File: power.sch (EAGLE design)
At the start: 26 parts

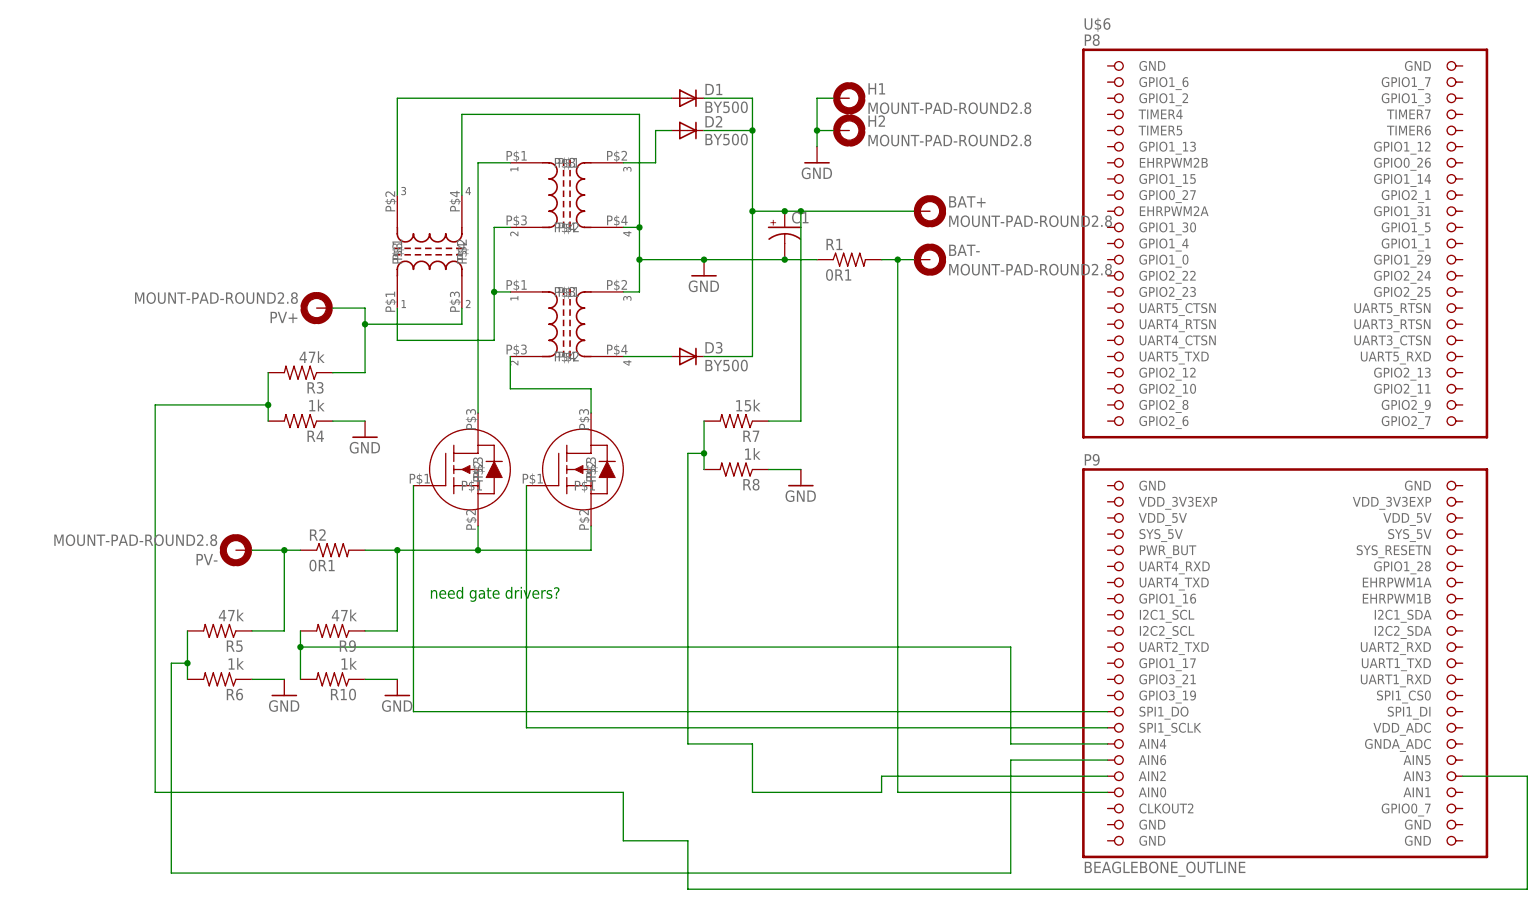
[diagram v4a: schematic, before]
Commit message: better ground paths
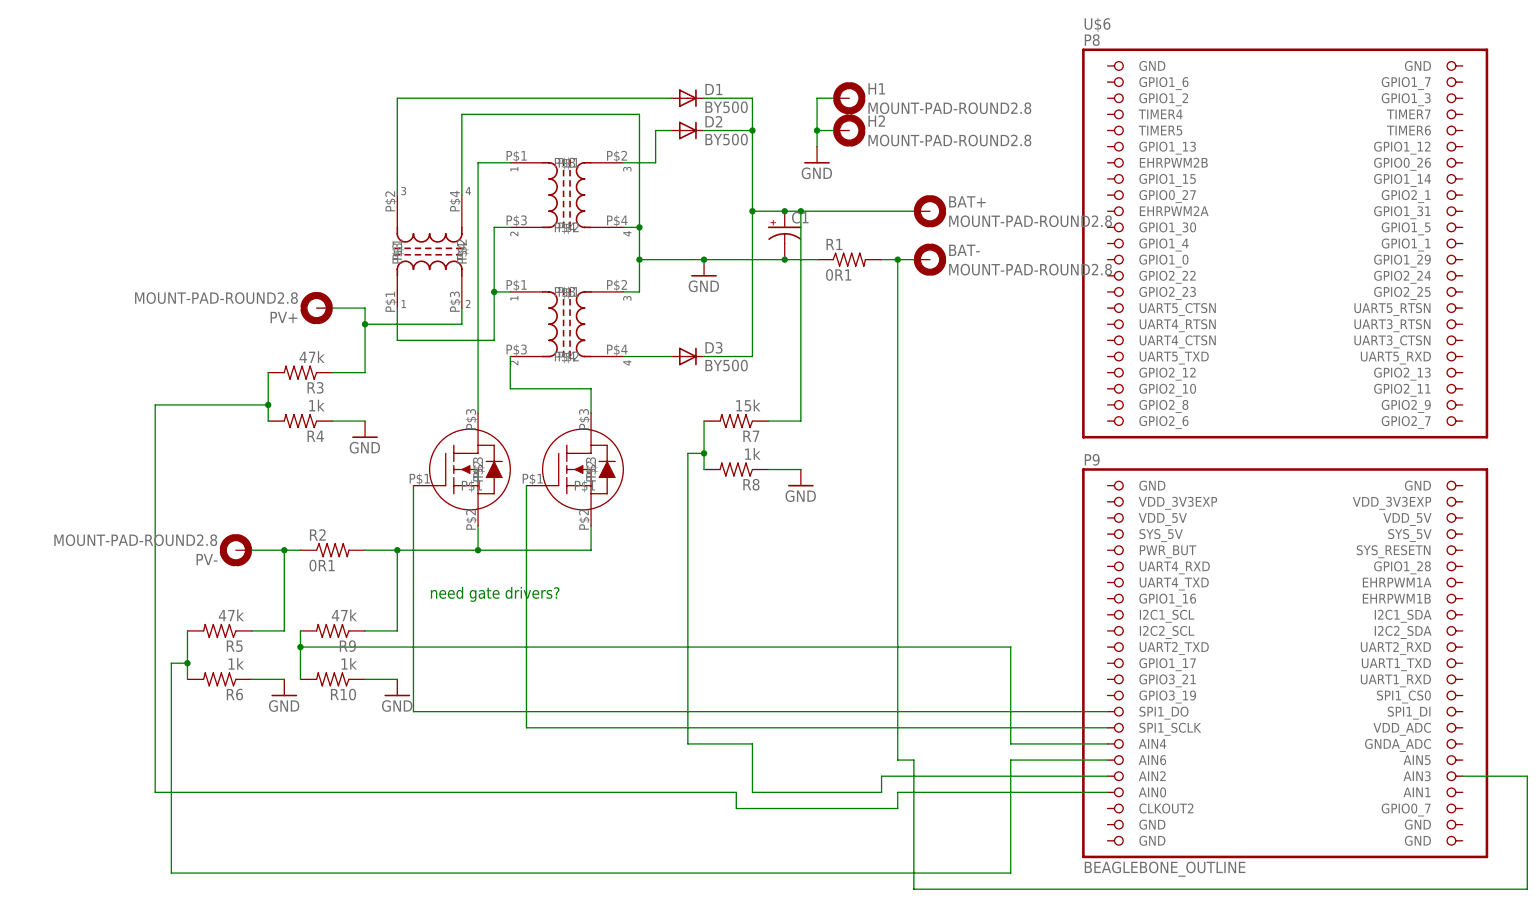
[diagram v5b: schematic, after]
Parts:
- C1: device rcl:CPOL-USE3.5-8 -> rcl:CPOL-USE5-10.5
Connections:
- net N$12: now also R3.2, R4.2; no longer BAT-.MOUNT, R1.2
- net N$4: now also BAT-.MOUNT, R1.2; no longer R3.2, R4.2
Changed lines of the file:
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@@
 <grid distance="0.1" unitdist="inch" unit="inch" style="lines" multiple="1" display="no" altdistance="0.01" altunitdist="inch" altunit="inch"/>
 <layers>
-<layer number="1" name="Top" color="4" fill="1" visible="no" active="no"/>
-<layer number="16" name="Bottom" color="1" fill="1" visible="no" active="no"/>
-<layer number="17" name="Pads" color="2" fill="1" visible="no" active="no"/>
-<layer number="18" name="Vias" color="2" fill="1" visible="no" active="no"/>
-<layer number="19" name="Unrouted" color="6" fill="1" visible="no" active="no"/>
-<layer number="20" name="Dimension" color="15" fill="1" visible="no" active="no"/>
-<layer number="21" name="tPlace" color="7" fill="1" visible="no" active="no"/>
-<layer number="22" name="bPlace" color="7" fill="1" visible="no" active="no"/>
-<layer number="23" name="tOrigins" color="15" fill="1" visible="no" active="no"/>
-<layer number="24" name="bOrigins" color="15" fill="1" visible="no" active="no"/>
-<layer number="25" name="tNames" color="7" fill="1" visible="no" active="no"/>
-<layer number="26" name="bNames" color="7" fill="1" visible="no" active="no"/>
-<layer number="27" name="tValues" color="7" fill="1" visible="no" active="no"/>
-<layer number="28" name="bValues" color="7" fill="1" visible="no" active="no"/>
+<layer number="1" name="Top" color="4" fill="1" visible="yes" active="no"/>
+<layer number="16" name="Bottom" color="1" fill="1" visible="yes" active="no"/>
+<layer number="17" name="Pads" color="2" fill="1" visible="yes" active="no"/>
+<layer number="18" name="Vias" color="2" fill="1" visible="yes" active="no"/>
+<layer number="19" name="Unrouted" color="6" fill="1" visible="yes" active="no"/>
+<layer number="20" name="Dimension" color="15" fill="1" visible="yes" active="no"/>
+<layer number="21" name="tPlace" color="7" fill="1" visible="yes" active="no"/>
+<layer number="22" name="bPlace" color="7" fill="1" visible="yes" active="no"/>
+<layer number="23" name="tOrigins" color="15" fill="1" visible="yes" active="no"/>
+<layer number="24" name="bOrigins" color="15" fill="1" visible="yes" active="no"/>
+<layer number="25" name="tNames" color="7" fill="1" visible="yes" active="no"/>
+<layer number="26" name="bNames" color="7" fill="1" visible="yes" active="no"/>
+<layer number="27" name="tValues" color="7" fill="1" visible="yes" active="no"/>
+<layer number="28" name="bValues" color="7" fill="1" visible="yes" active="no"/>
 <layer number="29" name="tStop" color="7" fill="3" visible="no" active="no"/>
 <layer number="30" name="bStop" color="7" fill="6" visible="no" active="no"/>
@@
 <layer number="35" name="tGlue" color="7" fill="4" visible="no" active="no"/>
 <layer number="36" name="bGlue" color="7" fill="5" visible="no" active="no"/>
-<layer number="37" name="tTest" color="7" fill="1" visible="no" active="no"/>
-<layer number="38" name="bTest" color="7" fill="1" visible="no" active="no"/>
+<layer number="37" name="tTest" color="7" fill="1" visible="yes" active="no"/>
+<layer number="38" name="bTest" color="7" fill="1" visible="yes" active="no"/>
 <layer number="39" name="tKeepout" color="4" fill="11" visible="no" active="no"/>
 <layer number="40" name="bKeepout" color="1" fill="11" visible="no" active="no"/>
@@
 <layer number="44" name="Drills" color="7" fill="1" visible="no" active="no"/>
 <layer number="45" name="Holes" color="7" fill="1" visible="no" active="no"/>
-<layer number="46" name="Milling" color="3" fill="1" visible="no" active="no"/>
-<layer number="47" name="Measures" color="7" fill="1" visible="no" active="no"/>
-<layer number="48" name="Document" color="7" fill="1" visible="no" active="no"/>
-<layer number="49" name="Reference" color="7" fill="1" visible="no" active="no"/>
-<layer number="50" name="dxf" color="7" fill="1" visible="no" active="no"/>
-<layer number="51" name="tDocu" color="7" fill="1" visible="no" active="no"/>
-<layer number="52" name="bDocu" color="7" fill="1" visible="no" active="no"/>
-<layer number="53" name="tGND_GNDA" color="7" fill="9" visible="no" active="no"/>
-<layer number="54" name="bGND_GNDA" color="1" fill="9" visible="no" active="no"/>
-<layer number="56" name="wert" color="7" fill="1" visible="no" active="no"/>
-<layer number="57" name="tCAD" color="7" fill="1" visible="no" active="no"/>
+<layer number="46" name="Milling" color="3" fill="1" visible="yes" active="no"/>
+<layer number="47" name="Measures" color="7" fill="1" visible="yes" active="no"/>
+<layer number="48" name="Document" color="7" fill="1" visible="yes" active="no"/>
+<layer number="49" name="Reference" color="7" fill="1" visible="yes" active="no"/>
+<layer number="50" name="dxf" color="7" fill="1" visible="yes" active="no"/>
+<layer number="51" name="tDocu" color="7" fill="1" visible="yes" active="no"/>
+<layer number="52" name="bDocu" color="7" fill="1" visible="yes" active="no"/>
+<layer number="53" name="tGND_GNDA" color="7" fill="9" visible="yes" active="no"/>
+<layer number="54" name="bGND_GNDA" color="1" fill="9" visible="yes" active="no"/>
+<layer number="56" name="wert" color="7" fill="1" visible="yes" active="no"/>
+<layer number="57" name="tCAD" color="7" fill="1" visible="yes" active="no"/>
 <layer number="91" name="Nets" color="2" fill="1" visible="yes" active="yes"/>
 <layer number="92" name="Busses" color="1" fill="1" visible="yes" active="yes"/>
@@
 <part name="D2" library="diode" deviceset="BY500" device=""/>
 <part name="D3" library="diode" deviceset="BY500" device=""/>
-<part name="C1" library="rcl" deviceset="CPOL-US" device="E3.5-8"/>
+<part name="C1" library="rcl" deviceset="CPOL-US" device="E5-10.5"/>
 <part name="U$1" library="mjg" deviceset="FDB6670AL" device=""/>
 <part name="U$2" library="mjg" deviceset="FDB6670AL" device=""/>
@@
 <net name="N$4" class="0">
 <segment>
-<pinref part="R3" gate="G$1" pin="2"/>
-<pinref part="R4" gate="G$1" pin="2"/>
-<wire x1="-7.62" y1="33.02" x2="-7.62" y2="27.94" width="0.1524" layer="91"/>
-<wire x1="-7.62" y1="27.94" x2="-7.62" y2="25.4" width="0.1524" layer="91"/>
-<wire x1="-7.62" y1="27.94" x2="-25.4" y2="27.94" width="0.1524" layer="91"/>
-<wire x1="-25.4" y1="27.94" x2="-25.4" y2="-33.02" width="0.1524" layer="91"/>
-<junction x="-7.62" y="27.94"/>
-<wire x1="-25.4" y1="-33.02" x2="48.26" y2="-33.02" width="0.1524" layer="91"/>
-<wire x1="58.42" y1="-40.64" x2="58.42" y2="-48.26" width="0.1524" layer="91"/>
-<wire x1="58.42" y1="-48.26" x2="190.5" y2="-48.26" width="0.1524" layer="91"/>
 <pinref part="U$6" gate="G$1" pin="AIN3"/>
+<wire x1="93.98" y1="-48.26" x2="190.5" y2="-48.26" width="0.1524" layer="91"/>
 <wire x1="190.5" y1="-48.26" x2="190.5" y2="-30.48" width="0.1524" layer="91"/>
 <wire x1="190.5" y1="-30.48" x2="180.34" y2="-30.48" width="0.1524" layer="91"/>
-<wire x1="48.26" y1="-33.02" x2="48.26" y2="-40.64" width="0.1524" layer="91"/>
-<wire x1="48.26" y1="-40.64" x2="58.42" y2="-40.64" width="0.1524" layer="91"/>
+<pinref part="BAT-" gate="G$1" pin="MOUNT"/>
+<pinref part="R1" gate="G$1" pin="2"/>
+<wire x1="88.9" y1="50.8" x2="91.44" y2="50.8" width="0.1524" layer="91"/>
+<wire x1="91.44" y1="50.8" x2="93.98" y2="50.8" width="0.1524" layer="91"/>
+<junction x="91.44" y="50.8"/>
+<wire x1="91.44" y1="50.8" x2="91.44" y2="-27.94" width="0.1524" layer="91"/>
+<wire x1="91.44" y1="-27.94" x2="93.98" y2="-27.94" width="0.1524" layer="91"/>
+<wire x1="93.98" y1="-27.94" x2="93.98" y2="-48.26" width="0.1524" layer="91"/>
 </segment>
 </net>
@@
 </segment>
 </net>
-<net name="N$12" class="0">
-<segment>
-<pinref part="U$6" gate="G$1" pin="AIN0"/>
-<wire x1="91.44" y1="-33.02" x2="124.46" y2="-33.02" width="0.1524" layer="91"/>
-<pinref part="BAT-" gate="G$1" pin="MOUNT"/>
-<pinref part="R1" gate="G$1" pin="2"/>
-<wire x1="88.9" y1="50.8" x2="91.44" y2="50.8" width="0.1524" layer="91"/>
-<wire x1="91.44" y1="50.8" x2="93.98" y2="50.8" width="0.1524" layer="91"/>
-<junction x="91.44" y="50.8"/>
-<wire x1="91.44" y1="50.8" x2="91.44" y2="-33.02" width="0.1524" layer="91"/>
-</segment>
-</net>
 <net name="N$10" class="0">
 <segment>
@@
 </segment>
 </net>
+<net name="N$12" class="0">
+<segment>
+<pinref part="U$6" gate="G$1" pin="AIN0"/>
+<wire x1="91.44" y1="-33.02" x2="124.46" y2="-33.02" width="0.1524" layer="91"/>
+<wire x1="91.44" y1="-35.56" x2="91.44" y2="-33.02" width="0.1524" layer="91"/>
+<wire x1="66.04" y1="-35.56" x2="91.44" y2="-35.56" width="0.1524" layer="91"/>
+<wire x1="66.04" y1="-33.02" x2="66.04" y2="-35.56" width="0.1524" layer="91"/>
+<wire x1="-25.4" y1="-33.02" x2="66.04" y2="-33.02" width="0.1524" layer="91"/>
+<pinref part="R4" gate="G$1" pin="2"/>
+<pinref part="R3" gate="G$1" pin="2"/>
+<wire x1="-7.62" y1="33.02" x2="-7.62" y2="27.94" width="0.1524" layer="91"/>
+<wire x1="-7.62" y1="27.94" x2="-7.62" y2="25.4" width="0.1524" layer="91"/>
+<junction x="-7.62" y="27.94"/>
+<wire x1="-7.62" y1="27.94" x2="-25.4" y2="27.94" width="0.1524" layer="91"/>
+<wire x1="-25.4" y1="27.94" x2="-25.4" y2="-33.02" width="0.1524" layer="91"/>
+</segment>
+</net>

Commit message: fixed a lot of things.  confidence that this could work is up to 1%.
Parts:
- removed H2: MOUNT-PAD-ROUND2.8, holes:MOUNT-PAD-ROUND2.8
- removed R7: 15k, rcl:R-US_R0603
- removed U$1, U$2: FDB6670AL, mjg:FDB6670AL
- added U$7, U$8: 45NO6LG, semiconductors:45NO6LG
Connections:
- net GND: no longer H2.MOUNT
- net N$10: no longer R7.2
- net N$11: now also U$6.SPI1_DO, U$8.G; no longer U$2.P$1, U$6.SPI1_SCLK
- net N$13: now also U$6.SPI1_SCLK, U$7.G; no longer U$1.P$1, U$6.SPI1_DO
- net N$15: now also U$7.D; no longer U$1.P$2
- net N$5: now also U$8.D; no longer U$2.P$2
- net N$7: no longer R7.1
- net N$8: now also U$8.S; no longer U$1.P$3, U$2.P$3
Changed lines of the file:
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@@
 <part name="D3" library="diode" deviceset="BY500" device=""/>
 <part name="C1" library="rcl" deviceset="CPOL-US" device="E5-10.5"/>
-<part name="U$1" library="mjg" deviceset="FDB6670AL" device=""/>
-<part name="U$2" library="mjg" deviceset="FDB6670AL" device=""/>
 <part name="R1" library="rcl" deviceset="R-US_" device="R0603" value="0R1"/>
 <part name="R2" library="rcl" deviceset="R-US_" device="R0603" value="0R1"/>
@@
 <part name="R6" library="rcl" deviceset="R-US_" device="R0603" value="1k"/>
 <part name="GND3" library="supply1" deviceset="GND" device=""/>
-<part name="R7" library="rcl" deviceset="R-US_" device="R0603" value="15k"/>
 <part name="R8" library="rcl" deviceset="R-US_" device="R0603" value="1k"/>
 <part name="GND4" library="supply1" deviceset="GND" device=""/>
@@
 <part name="BAT-" library="holes" deviceset="MOUNT-PAD-ROUND" device="2.8"/>
 <part name="H1" library="holes" deviceset="MOUNT-PAD-ROUND" device="2.8"/>
-<part name="H2" library="holes" deviceset="MOUNT-PAD-ROUND" device="2.8"/>
 <part name="GND6" library="supply1" deviceset="GND" device=""/>
+<part name="U$7" library="semiconductors" deviceset="45NO6LG" device=""/>
+<part name="U$8" library="semiconductors" deviceset="45NO6LG" device=""/>
 </parts>
 <sheets>
@@
 <instance part="D3" gate="1" x="58.42" y="35.56"/>
 <instance part="C1" gate="G$1" x="73.66" y="55.88"/>
-<instance part="U$1" gate="G$1" x="24.13" y="17.78"/>
-<instance part="U$2" gate="G$1" x="41.91" y="17.78"/>
 <instance part="R1" gate="G$1" x="83.82" y="50.8"/>
 <instance part="R2" gate="G$1" x="2.54" y="5.08"/>
@@
 <instance part="R6" gate="G$1" x="-15.24" y="-15.24" rot="R180"/>
 <instance part="GND3" gate="1" x="-5.08" y="-17.78"/>
-<instance part="R7" gate="G$1" x="66.04" y="25.4" rot="R180"/>
 <instance part="R8" gate="G$1" x="66.04" y="17.78" rot="R180"/>
 <instance part="GND4" gate="1" x="76.2" y="15.24"/>
@@
 <instance part="BAT-" gate="G$1" x="96.52" y="50.8"/>
 <instance part="H1" gate="G$1" x="83.82" y="76.2"/>
-<instance part="H2" gate="G$1" x="83.82" y="71.12"/>
 <instance part="GND6" gate="1" x="78.74" y="66.04"/>
+<instance part="U$7" gate="G$1" x="22.86" y="17.78"/>
+<instance part="U$8" gate="G$1" x="40.64" y="17.78"/>
 </instances>
 <busses>
@@
 <net name="N$5" class="0">
 <segment>
-<pinref part="U$2" gate="G$1" pin="P$2"/>
-<wire x1="43.18" y1="26.67" x2="43.18" y2="30.48" width="0.1524" layer="91"/>
 <pinref part="U$4" gate="G$1" pin="P$2"/>
 <wire x1="30.48" y1="35.56" x2="30.48" y2="30.48" width="0.1524" layer="91"/>
 <wire x1="30.48" y1="30.48" x2="43.18" y2="30.48" width="0.1524" layer="91"/>
+<pinref part="U$8" gate="G$1" pin="D"/>
+<wire x1="43.18" y1="30.48" x2="43.18" y2="22.86" width="0.1524" layer="91"/>
 </segment>
 </net>
 <net name="N$13" class="0">
 <segment>
-<pinref part="U$1" gate="G$1" pin="P$1"/>
-<pinref part="U$6" gate="G$1" pin="SPI1_DO"/>
-<wire x1="15.24" y1="-20.32" x2="15.24" y2="15.24" width="0.1524" layer="91"/>
-<wire x1="124.46" y1="-20.32" x2="15.24" y2="-20.32" width="0.1524" layer="91"/>
+<wire x1="15.24" y1="-22.86" x2="15.24" y2="15.24" width="0.1524" layer="91"/>
+<pinref part="U$7" gate="G$1" pin="G"/>
+<wire x1="15.24" y1="15.24" x2="20.32" y2="15.24" width="0.1524" layer="91"/>
+<pinref part="U$6" gate="G$1" pin="SPI1_SCLK"/>
+<wire x1="124.46" y1="-22.86" x2="15.24" y2="-22.86" width="0.1524" layer="91"/>
 </segment>
 </net>
@@
 <pinref part="U$5" gate="G$1" pin="P$1"/>
 <wire x1="30.48" y1="66.04" x2="25.4" y2="66.04" width="0.1524" layer="91"/>
-<pinref part="U$1" gate="G$1" pin="P$2"/>
-<wire x1="25.4" y1="66.04" x2="25.4" y2="26.67" width="0.1524" layer="91"/>
+<wire x1="25.4" y1="66.04" x2="25.4" y2="22.86" width="0.1524" layer="91"/>
+<pinref part="U$7" gate="G$1" pin="D"/>
 </segment>
 </net>
@@
 <wire x1="81.28" y1="76.2" x2="78.74" y2="76.2" width="0.1524" layer="91"/>
 <wire x1="78.74" y1="76.2" x2="78.74" y2="71.12" width="0.1524" layer="91"/>
-<pinref part="H2" gate="G$1" pin="MOUNT"/>
 <wire x1="78.74" y1="71.12" x2="78.74" y2="68.58" width="0.1524" layer="91"/>
 <wire x1="81.28" y1="71.12" x2="78.74" y2="71.12" width="0.1524" layer="91"/>
@@
 <net name="N$7" class="0">
 <segment>
-<pinref part="R7" gate="G$1" pin="1"/>
 <wire x1="76.2" y1="25.4" x2="71.12" y2="25.4" width="0.1524" layer="91"/>
 <pinref part="D1" gate="1" pin="C"/>
@@
 <pinref part="R9" gate="G$1" pin="1"/>
 <wire x1="12.7" y1="-7.62" x2="7.62" y2="-7.62" width="0.1524" layer="91"/>
-<pinref part="U$1" gate="G$1" pin="P$3"/>
-<wire x1="25.4" y1="8.89" x2="25.4" y2="5.08" width="0.1524" layer="91"/>
-<wire x1="25.4" y1="5.08" x2="43.18" y2="5.08" width="0.1524" layer="91"/>
-<pinref part="U$2" gate="G$1" pin="P$3"/>
-<wire x1="43.18" y1="5.08" x2="43.18" y2="8.89" width="0.1524" layer="91"/>
-<wire x1="25.4" y1="5.08" x2="12.7" y2="5.08" width="0.1524" layer="91"/>
-<junction x="25.4" y="5.08"/>
+<wire x1="12.7" y1="5.08" x2="43.18" y2="5.08" width="0.1524" layer="91"/>
 <pinref part="R2" gate="G$1" pin="2"/>
 <wire x1="12.7" y1="5.08" x2="7.62" y2="5.08" width="0.1524" layer="91"/>
 <wire x1="12.7" y1="-7.62" x2="12.7" y2="5.08" width="0.1524" layer="91"/>
 <junction x="12.7" y="5.08"/>
+<pinref part="U$8" gate="G$1" pin="S"/>
+<wire x1="43.18" y1="12.7" x2="43.18" y2="5.08" width="0.1524" layer="91"/>
 </segment>
 </net>
@@
 <net name="N$11" class="0">
 <segment>
-<pinref part="U$2" gate="G$1" pin="P$1"/>
-<wire x1="33.02" y1="-22.86" x2="33.02" y2="15.24" width="0.1524" layer="91"/>
-<pinref part="U$6" gate="G$1" pin="SPI1_SCLK"/>
-<wire x1="33.02" y1="-22.86" x2="124.46" y2="-22.86" width="0.1524" layer="91"/>
+<wire x1="33.02" y1="-20.32" x2="33.02" y2="15.24" width="0.1524" layer="91"/>
+<pinref part="U$8" gate="G$1" pin="G"/>
+<wire x1="38.1" y1="15.24" x2="33.02" y2="15.24" width="0.1524" layer="91"/>
+<pinref part="U$6" gate="G$1" pin="SPI1_DO"/>
+<wire x1="33.02" y1="-20.32" x2="124.46" y2="-20.32" width="0.1524" layer="91"/>
 </segment>
 </net>
@@
 <wire x1="68.58" y1="-25.4" x2="68.58" y2="-33.02" width="0.1524" layer="91"/>
 <pinref part="R8" gate="G$1" pin="2"/>
-<pinref part="R7" gate="G$1" pin="2"/>
 <wire x1="60.96" y1="25.4" x2="60.96" y2="20.32" width="0.1524" layer="91"/>
 <wire x1="60.96" y1="20.32" x2="60.96" y2="17.78" width="0.1524" layer="91"/>
